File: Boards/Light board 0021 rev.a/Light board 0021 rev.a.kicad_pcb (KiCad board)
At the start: 2 copper layers, 166.4 x 186.7 mm, 44 parts, among them J1 card edge, J2 light connector, Q1 2N6125, U1 2.2K, U14 Unused DIP, U16 Unused DIP, U2 2.2K, U3 ULN2003A, U4 ULN2003A, U5 7406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

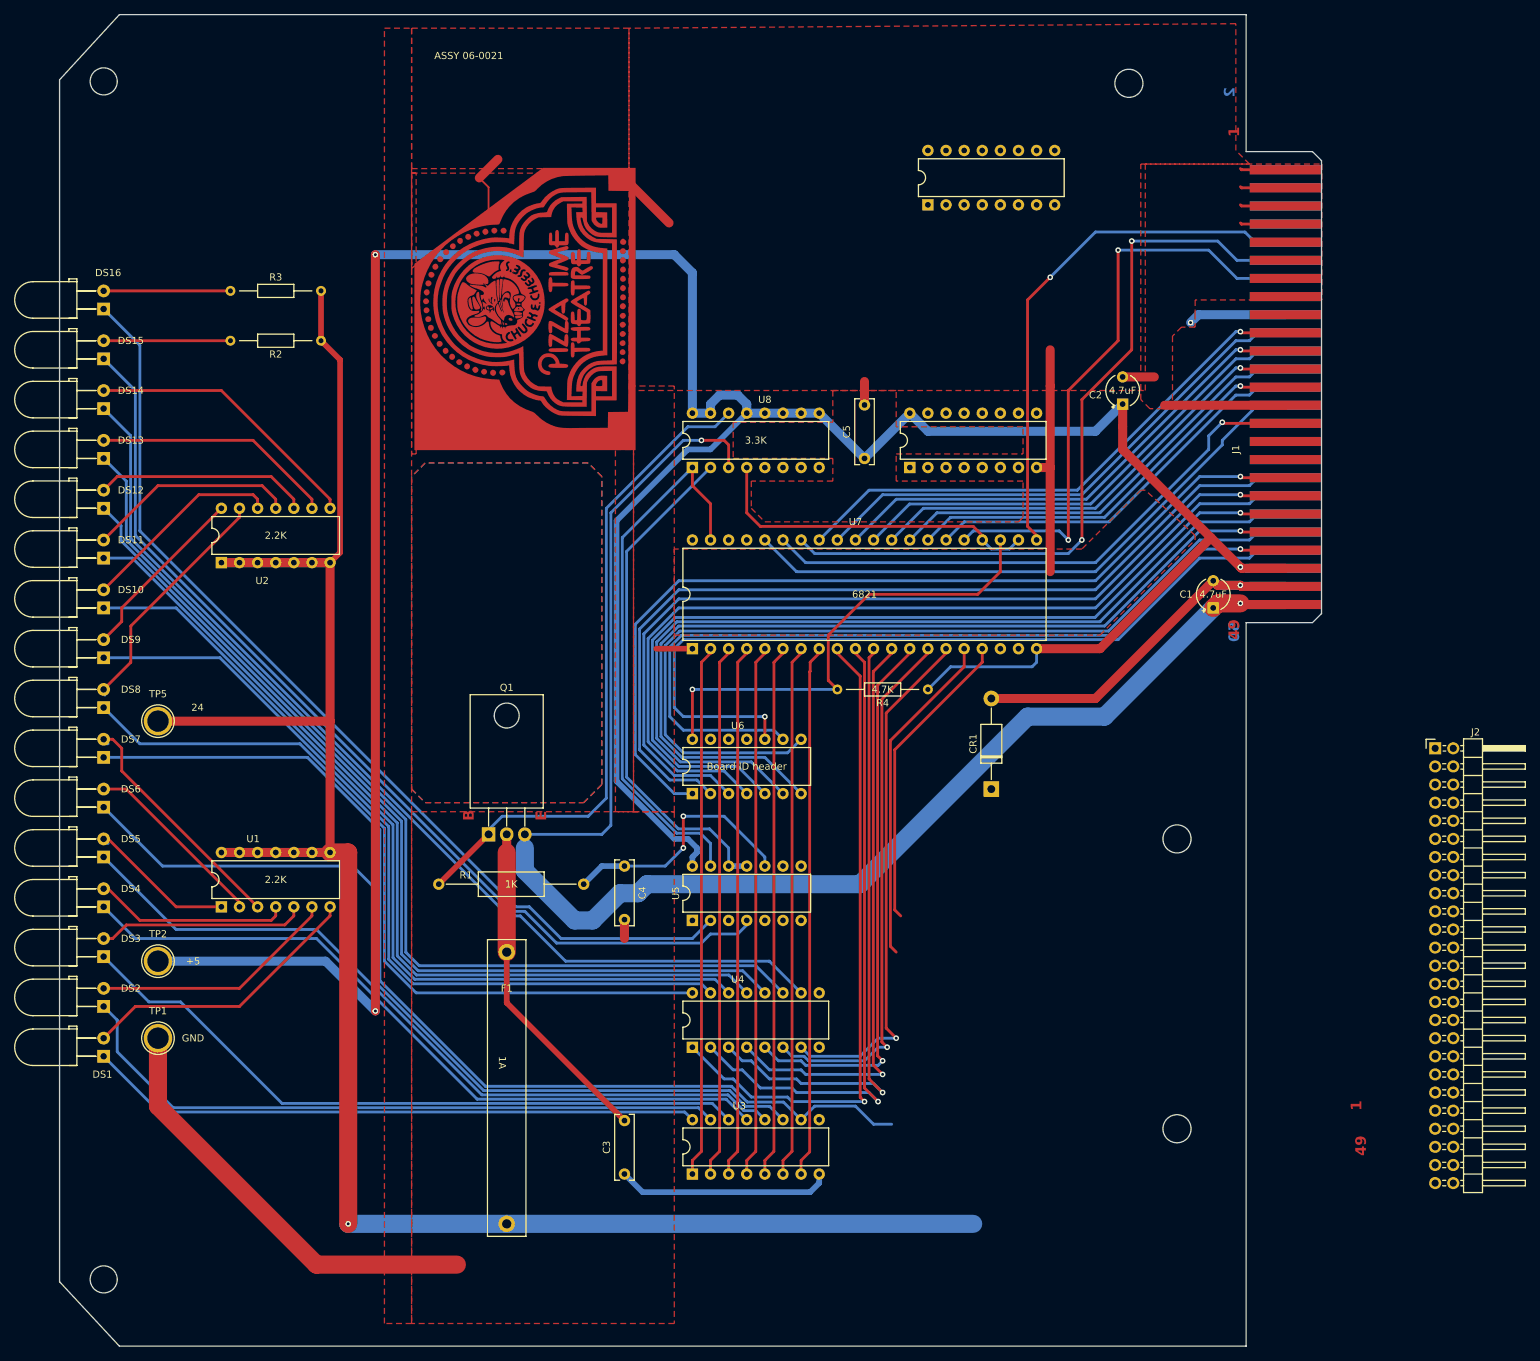
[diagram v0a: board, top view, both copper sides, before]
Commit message: finish light board rev.a, rename files, add renders and schematics, move pictures
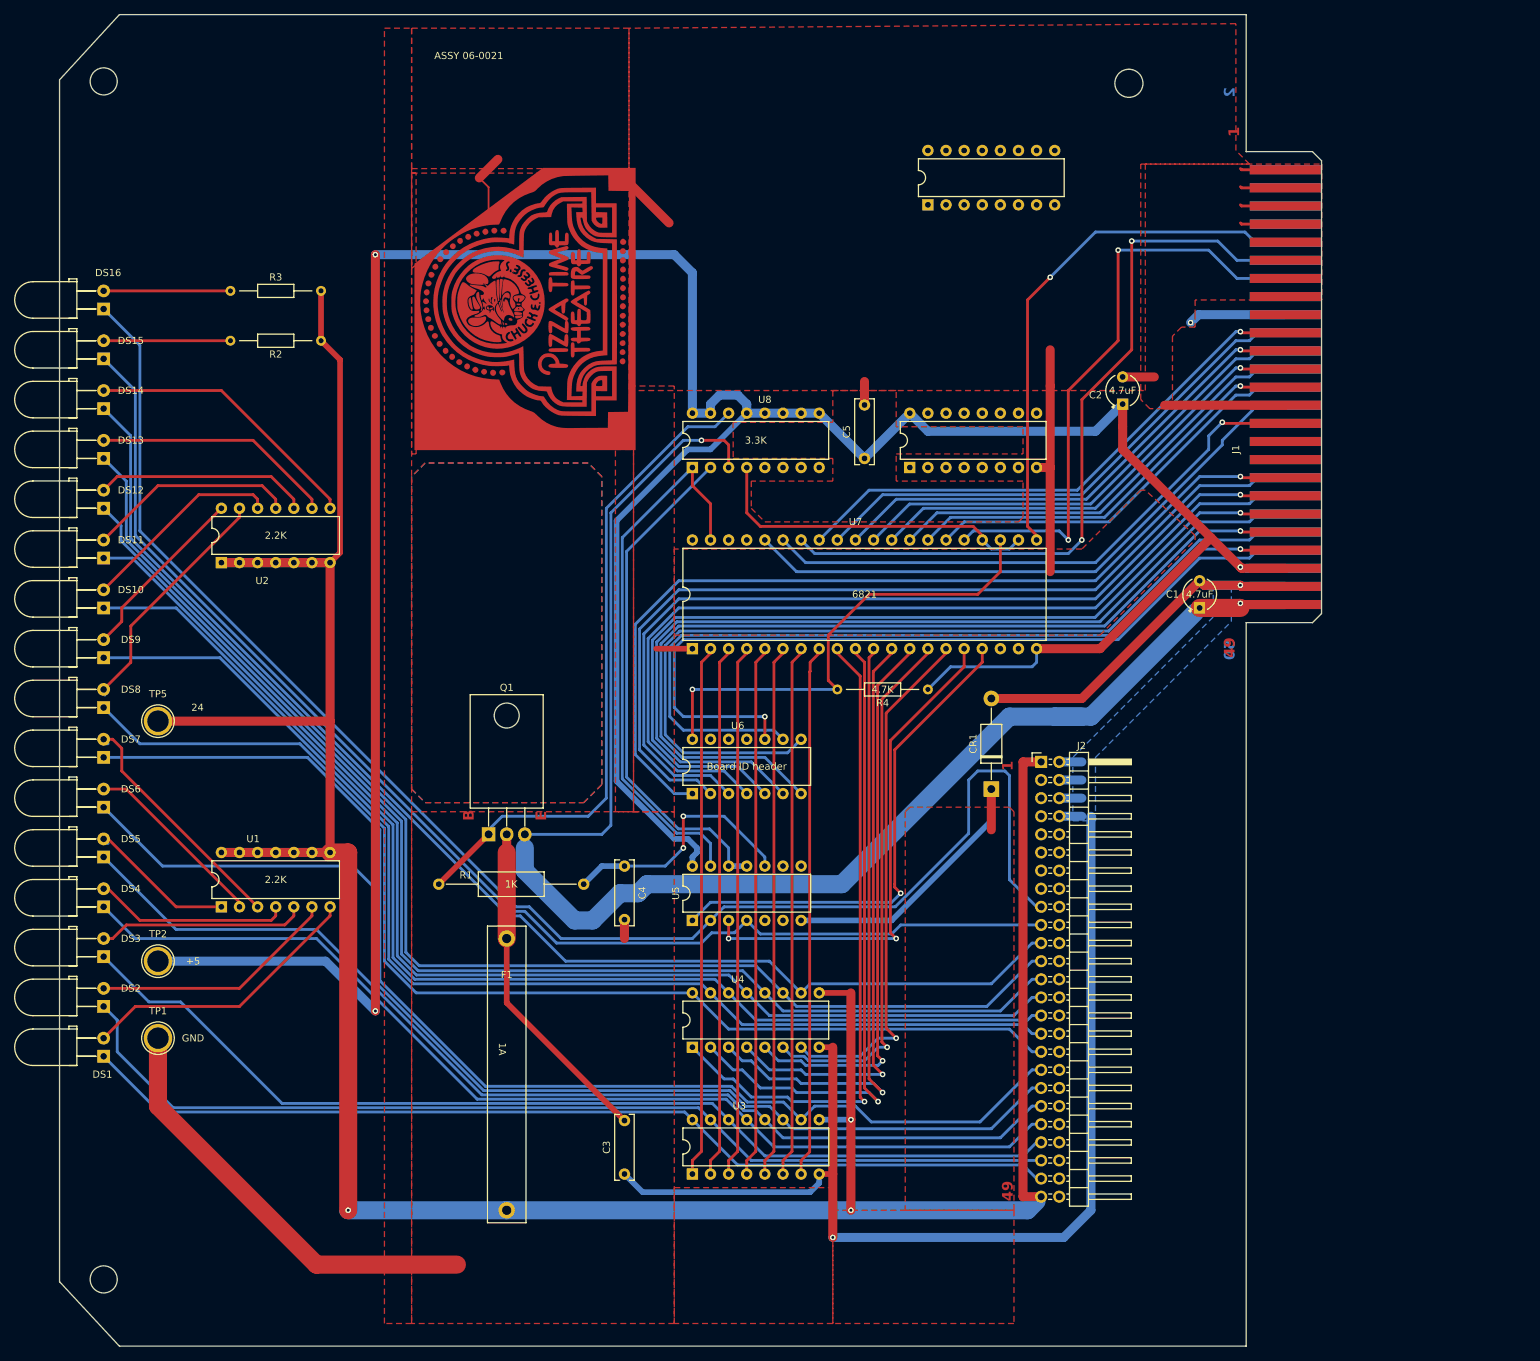
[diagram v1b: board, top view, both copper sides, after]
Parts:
- moved J2 55.3 mm to (155.6, 104.8)
- moved C1 1.91 mm to (177.8, 83.2)
- moved F1 1.91 mm to (80.6, 129.5)
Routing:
- net 24R: track 89.0 -> 227.1 mm, vias 1 -> 2
- net 24Vout: track 307.6 -> 421.4 mm, vias 1 -> 3
- net B7out: track 138.0 -> 213.8 mm
- net A7out: track 110.0 -> 162.3 mm
- net A0out: track 86.2 -> 138.5 mm
- net B0out: track 115.5 -> 164.2 mm
- net A1out: track 94.3 -> 143.0 mm
- net A2out: track 97.1 -> 143.8 mm
- net B1out: track 120.9 -> 166.6 mm
- net A3out: track 102.5 -> 146.7 mm
- net B2out: track 126.3 -> 170.0 mm
- net GND: track 182.5 -> 225.1 mm
- net B6out: track 137.7 -> 179.9 mm
- net B3out: track 133.0 -> 174.6 mm
- net A4out: track 108.0 -> 149.6 mm
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- added copper zone on B.Cu, net 24R
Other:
- outline, holes or cut-outs redrawn

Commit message: revisions from real life boards
tip130a is actually tip30a, widened holes for crystal, widened holes for big power resistor, fixed cpu board LED resistors
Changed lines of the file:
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@@
     (fp_line (start 20.32 0) (end 14.66 0)
       (stroke (width 0.1) (type solid)) (layer "F.Fab"))
-    (pad "1" thru_hole circle (at 0 0) (size 1.6 1.6) (drill 0.8) (layers "*.Cu" "*.Mask")
+    (pad "1" thru_hole circle (at 0 0) (size 2 2) (drill 1) (layers "*.Cu" "*.Mask")
       (net 102 "24Vpu") (pintype "passive"))
-    (pad "2" thru_hole oval (at 20.32 0) (size 1.6 1.6) (drill 0.8) (layers "*.Cu" "*.Mask")
+    (pad "2" thru_hole circle (at 20.32 0) (size 2 2) (drill 1) (layers "*.Cu" "*.Mask")
       (net 6 "Net-(C4-Pad1)") (pintype "passive"))
     (model "${KICAD6_3DMODEL_DIR}/Resistor_THT.3dshapes/R_Axial_DIN0309_L9.0mm_D3.2mm_P20.32mm_Horizontal.wrl"

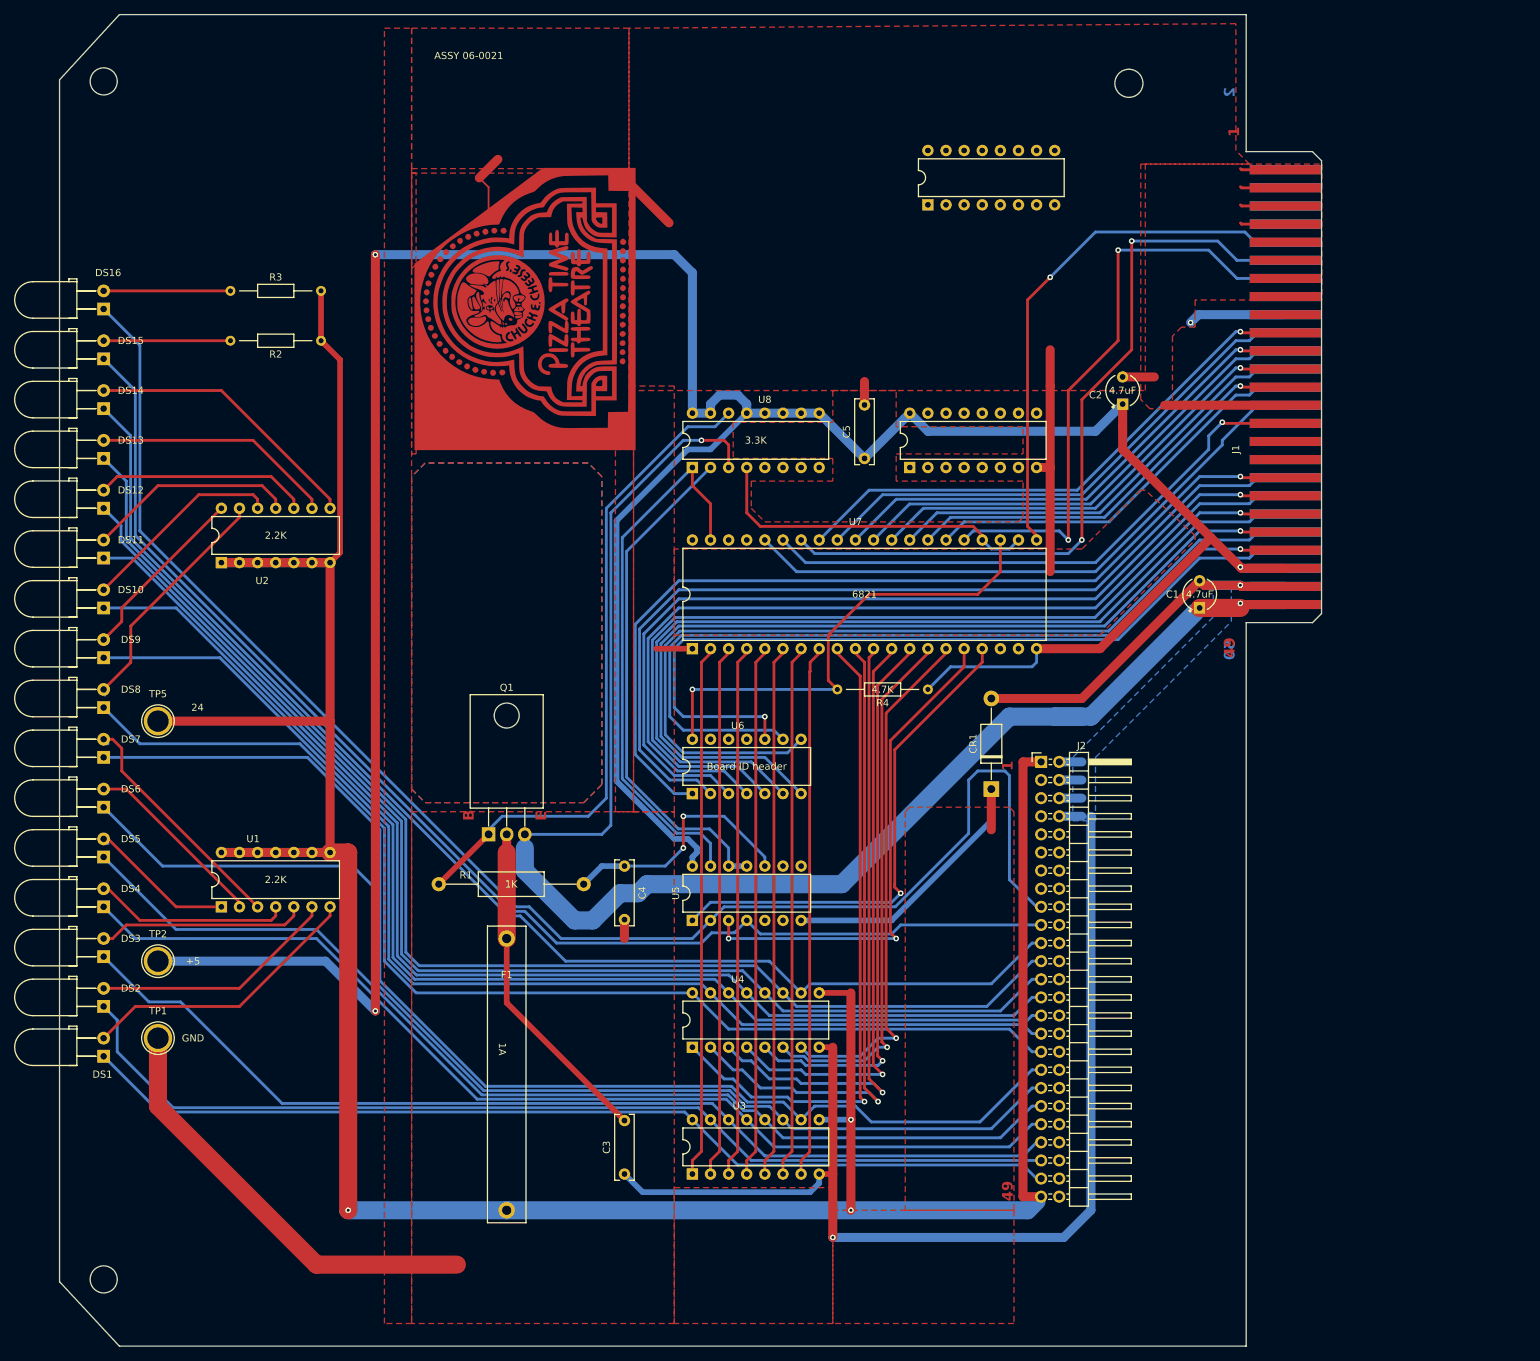
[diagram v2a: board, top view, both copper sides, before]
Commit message: revised PCBs based on Jen's boards, added rev.c
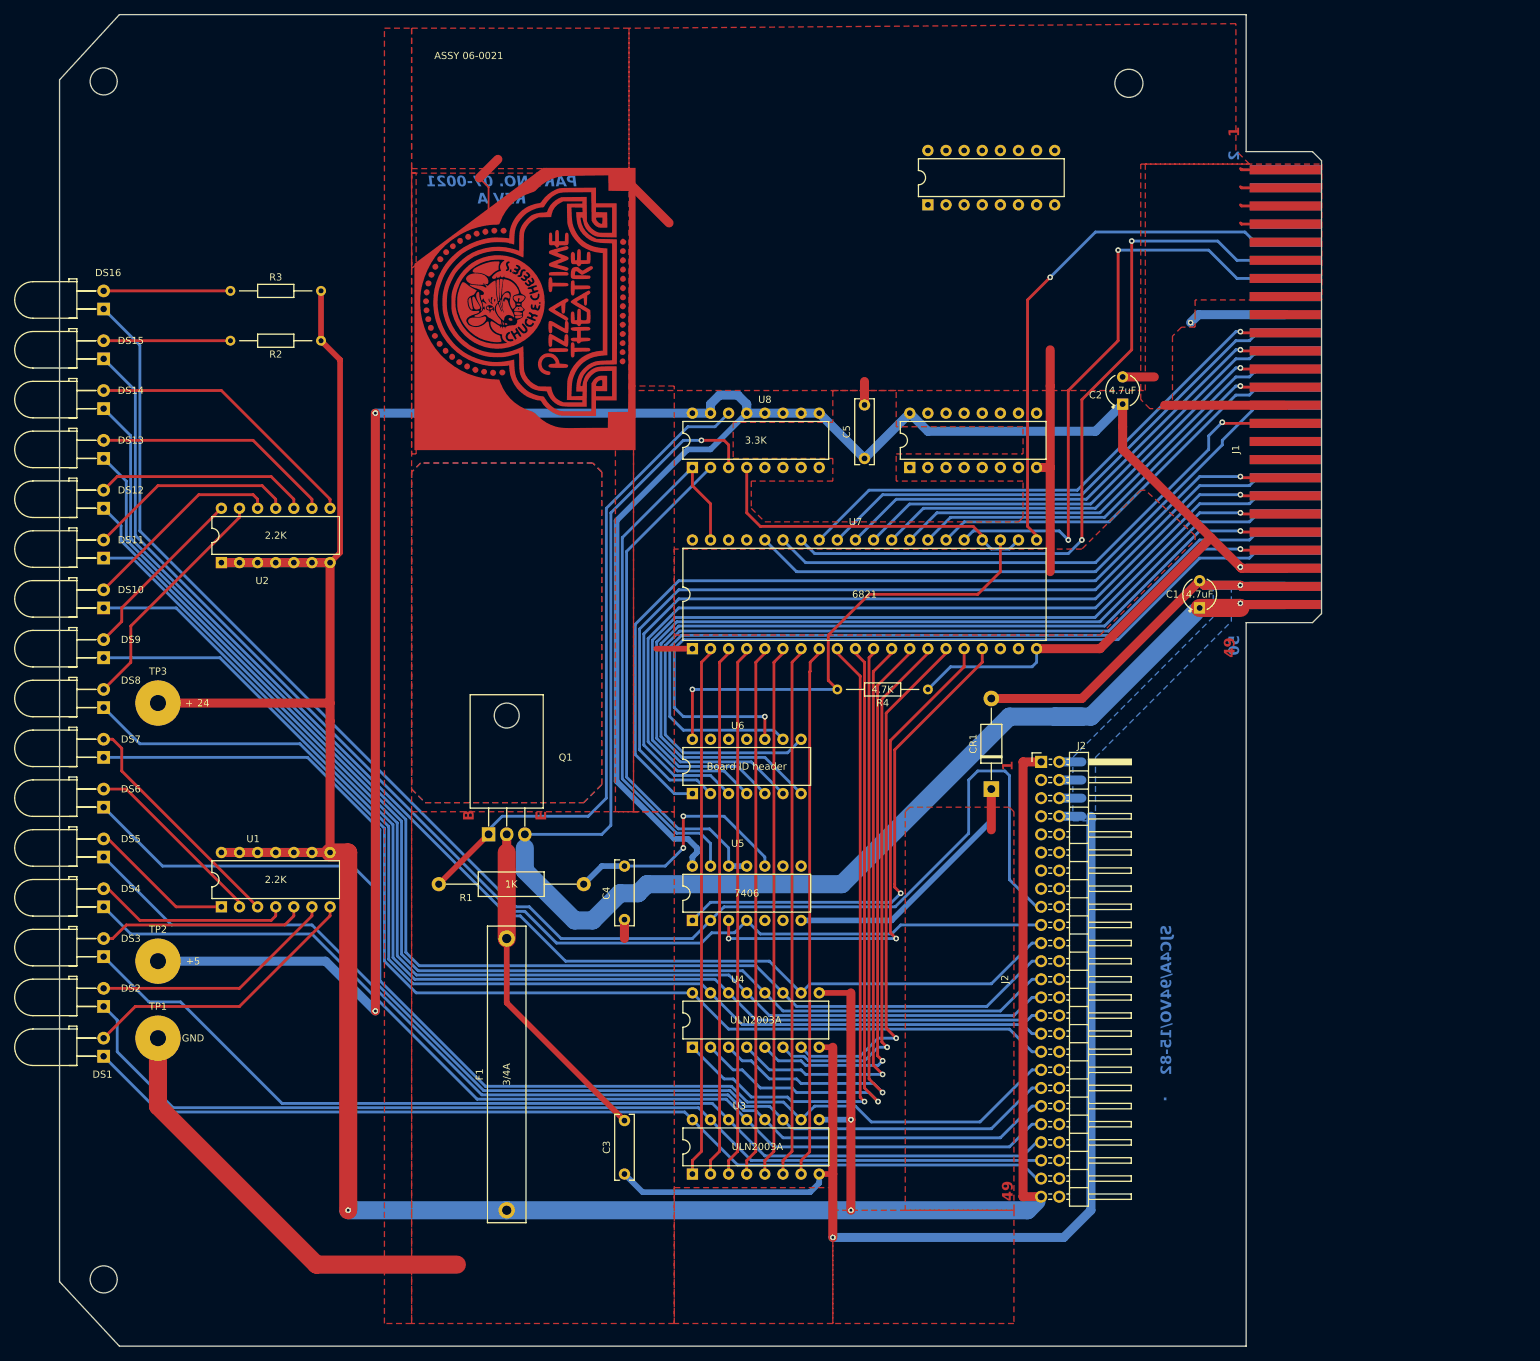
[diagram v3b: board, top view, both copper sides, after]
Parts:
- F1: value 1A -> 3/4A
- moved TP3 2.54 mm to (31.8, 96.5)
- renumbered TP5 to TP3
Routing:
- net 5V: track 446.6 -> 403.6 mm
- net unconnected-(U14-R3.1-Pad3): track 0.64 -> 0.00 mm
- net unconnected-(U16-R7.2-Pad10): track 0.63 -> 0.00 mm
- net CS: track 48.1 -> 47.5 mm
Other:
- board text added: "+"
- board text added: "."
- board text added: "PART NO. 07-0021 REV A"
- board text added: "SJC4A/94VO/15-82"
